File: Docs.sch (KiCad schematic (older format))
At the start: 0 parts

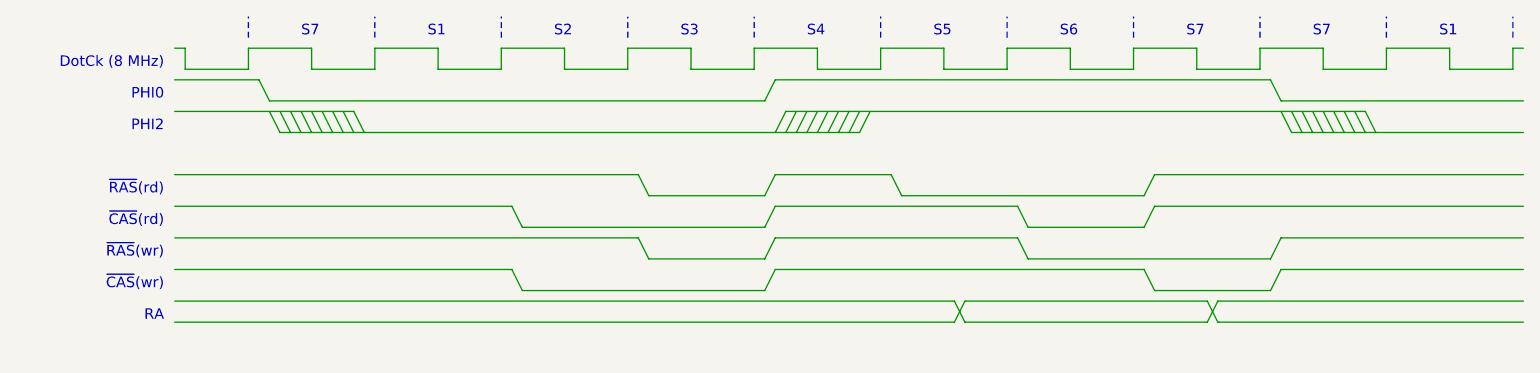
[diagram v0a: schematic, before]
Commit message: Updated timing diagram
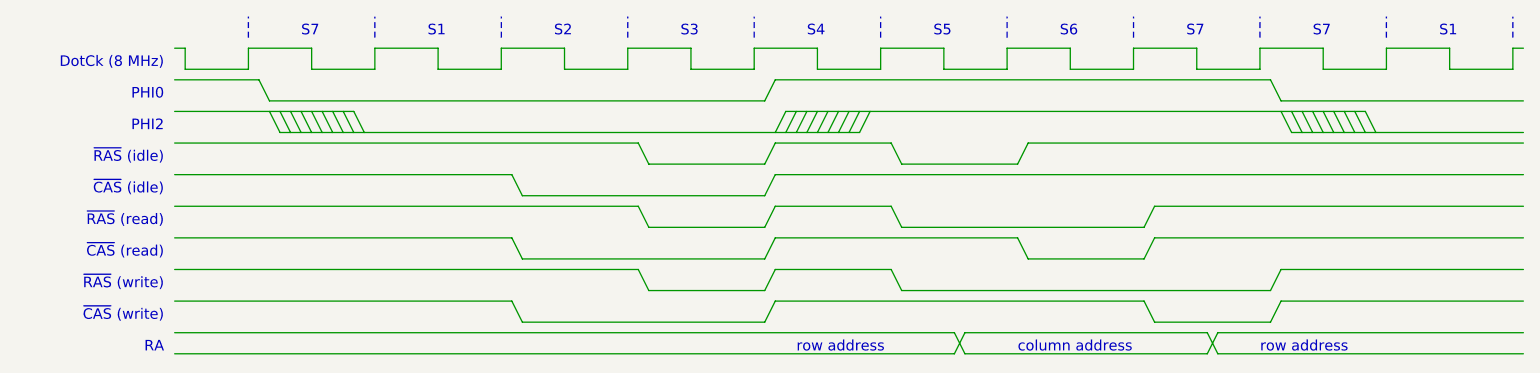
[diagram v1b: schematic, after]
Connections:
- wire segments 129 -> 143
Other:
- note added: "column address"
- note added: "row address"
- note added: "~CAS~ (idle)"
- note added: "~CAS~ (read)"
- note added: "~CAS~ (write)"
- note added: "~RAS~ (idle)"
- note added: "~RAS~ (read)"
- note added: "~RAS~ (write)"
- note removed: "~CAS~(rd)"
- note removed: "~CAS~(wr)"
- note removed: "~RAS~(rd)"
- note removed: "~RAS~(wr)"
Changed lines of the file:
@@
 Wire Wire Line
 	1100 1500 1950 1500
-Text Notes 1050 1900 2    50   ~ 0
-~RAS~(rd)
-Text Notes 1050 2050 2    50   ~ 0
-~CAS~(rd)
-Wire Wire Line
-	1100 1800 3300 1800
-Wire Wire Line
-	3300 1800 3350 1900
-Wire Wire Line
-	1100 1950 2700 1950
-Wire Wire Line
-	2700 1950 2750 2050
-Wire Wire Line
-	2750 2050 3900 2050
-Wire Wire Line
-	3900 2050 3950 1950
-Wire Wire Line
-	3350 1900 3900 1900
-Wire Wire Line
-	3900 1900 3950 1800
-Wire Wire Line
-	3950 1950 5100 1950
-Wire Wire Line
-	4500 1800 4550 1900
-Wire Wire Line
-	5100 1950 5150 2050
-Wire Wire Line
-	3950 1800 4500 1800
 Wire Notes Line
 	6850 1150 6850 1050
@@
 	6750 1500 6800 1600
 Wire Wire Line
-	5150 2050 5700 2050
-Wire Wire Line
-	5700 2050 5750 1950
-Wire Wire Line
-	4550 1900 5700 1900
-Wire Wire Line
-	5700 1900 5750 1800
-Text Notes 1050 2500 2    50   ~ 0
-RA
-Wire Wire Line
-	1100 2400 4800 2400
-Wire Wire Line
-	4800 2400 4850 2500
-Wire Wire Line
-	1100 2500 4800 2500
-Wire Wire Line
-	4800 2500 4850 2400
-Wire Wire Line
-	4850 2400 6000 2400
-Wire Wire Line
-	6000 2400 6050 2500
-Wire Wire Line
-	4850 2500 6000 2500
-Wire Wire Line
-	6050 2500 7500 2500
-Wire Wire Line
-	5750 1800 7500 1800
-Wire Wire Line
-	5750 1950 7500 1950
-Text Notes 1050 2200 2    50   ~ 0
-~RAS~(wr)
-Text Notes 1050 2350 2    50   ~ 0
-~CAS~(wr)
-Wire Wire Line
-	1100 2100 3300 2100
-Wire Wire Line
-	3300 2100 3350 2200
-Wire Wire Line
-	1100 2250 2700 2250
-Wire Wire Line
-	2700 2250 2750 2350
-Wire Wire Line
-	2750 2350 3900 2350
-Wire Wire Line
-	3900 2350 3950 2250
-Wire Wire Line
-	3350 2200 3900 2200
-Wire Wire Line
-	3900 2200 3950 2100
-Wire Wire Line
-	3950 2250 5700 2250
-Wire Wire Line
-	5700 2250 5750 2350
-Wire Wire Line
-	5750 2350 6300 2350
-Wire Wire Line
-	6300 2350 6350 2250
-Wire Wire Line
-	6300 2200 6350 2100
-Wire Wire Line
-	6350 2100 7500 2100
-Wire Wire Line
-	6350 2250 7500 2250
-Wire Wire Line
-	6050 2400 7500 2400
-Wire Wire Line
-	6000 2500 6050 2400
-Wire Wire Line
-	5150 2200 6300 2200
-Wire Wire Line
-	5100 2100 5150 2200
-Wire Wire Line
-	3950 2100 5100 2100
-Wire Wire Line
 	1700 1500 1750 1600
 Wire Wire Line
@@
 Wire Wire Line
 	6400 1600 7500 1600
+Wire Wire Line
+	3950 2250 4500 2250
+Wire Wire Line
+	4500 2250 4550 2350
+Wire Wire Line
+	4550 2350 6300 2350
+Wire Wire Line
+	6000 2650 6050 2550
+Wire Wire Line
+	6050 2550 7500 2550
+Wire Wire Line
+	6350 2400 7500 2400
+Wire Wire Line
+	6350 2250 7500 2250
+Wire Wire Line
+	6300 2350 6350 2250
+Wire Wire Line
+	6300 2500 6350 2400
+Wire Wire Line
+	5750 2500 6300 2500
+Wire Wire Line
+	5700 2400 5750 2500
+Wire Wire Line
+	3950 2400 5700 2400
+Wire Wire Line
+	3900 2350 3950 2250
+Wire Wire Line
+	3350 2350 3900 2350
+Wire Wire Line
+	3900 2500 3950 2400
+Wire Wire Line
+	2750 2500 3900 2500
+Wire Wire Line
+	2700 2400 2750 2500
+Wire Wire Line
+	1100 2400 2700 2400
+Wire Wire Line
+	3300 2250 3350 2350
+Wire Wire Line
+	1100 2250 3300 2250
+Text Notes 1050 2500 2    50   ~ 0
+~CAS~ (write)
+Text Notes 1050 2350 2    50   ~ 0
+~RAS~ (write)
+Wire Wire Line
+	5750 2100 7500 2100
+Wire Wire Line
+	5750 1950 7500 1950
+Wire Wire Line
+	6050 2650 7500 2650
+Wire Wire Line
+	4850 2650 6000 2650
+Wire Wire Line
+	6000 2550 6050 2650
+Wire Wire Line
+	4850 2550 6000 2550
+Wire Wire Line
+	4800 2650 4850 2550
+Wire Wire Line
+	1100 2650 4800 2650
+Wire Wire Line
+	4800 2550 4850 2650
+Wire Wire Line
+	1100 2550 4800 2550
+Text Notes 1050 2650 2    50   ~ 0
+RA
+Wire Wire Line
+	5700 2050 5750 1950
+Wire Wire Line
+	4550 2050 5700 2050
+Wire Wire Line
+	5700 2200 5750 2100
+Wire Wire Line
+	5150 2200 5700 2200
+Wire Wire Line
+	3950 1950 4500 1950
+Wire Wire Line
+	5100 2100 5150 2200
+Wire Wire Line
+	4500 1950 4550 2050
+Wire Wire Line
+	3950 2100 5100 2100
+Wire Wire Line
+	3900 2050 3950 1950
+Wire Wire Line
+	3350 2050 3900 2050
+Wire Wire Line
+	3900 2200 3950 2100
+Wire Wire Line
+	2750 2200 3900 2200
+Wire Wire Line
+	2700 2100 2750 2200
+Wire Wire Line
+	1100 2100 2700 2100
+Wire Wire Line
+	3300 1950 3350 2050
+Wire Wire Line
+	1100 1950 3300 1950
+Text Notes 1050 2200 2    50   ~ 0
+~CAS~ (read)
+Text Notes 1050 2050 2    50   ~ 0
+~RAS~ (read)
+Wire Wire Line
+	5150 1650 7500 1650
+Wire Wire Line
+	5100 1750 5150 1650
+Wire Wire Line
+	4550 1750 5100 1750
+Wire Wire Line
+	3950 1650 4500 1650
+Wire Wire Line
+	4500 1650 4550 1750
+Wire Wire Line
+	3900 1750 3950 1650
+Wire Wire Line
+	3350 1750 3900 1750
+Wire Wire Line
+	3900 1900 3950 1800
+Wire Wire Line
+	2750 1900 3900 1900
+Wire Wire Line
+	2700 1800 2750 1900
+Wire Wire Line
+	1100 1800 2700 1800
+Wire Wire Line
+	3300 1650 3350 1750
+Wire Wire Line
+	1100 1650 3300 1650
+Text Notes 1050 1750 2    50   ~ 0
+~RAS~ (idle)
+Text Notes 1050 1900 2    50   ~ 0
+~CAS~ (idle)
+Wire Wire Line
+	3950 1800 7500 1800
+Text Notes 4050 2650 0    50   ~ 0
+row address
+Text Notes 5100 2650 0    50   ~ 0
+column address
+Text Notes 6250 2650 0    50   ~ 0
+row address
 $EndSCHEMATC

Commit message: idk
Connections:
- wire segments 143 -> 247
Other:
- note added: "ACT"
- note added: "AREF"
- note added: "Command (read/idle)"
- note added: "Command (write)"
- note added: "NOP"
- note added: "PC all"
- note added: "PHI02r1"
- note added: "PHI02r2"
- note added: "PHI2e1"
- note added: "PHI2e2"
- note added: "PHI2e3"
- note added: "PHI2e4"
- note added: "PHI2e5"
- note added: "PHI2e6"
- note added: "PHI2e7"
- note added: "PHI2e8"
- note added: "RCS <= PHI2e7 || PHI2e8 || (Ref8 && (PHI2e3 || (PHI2e4 && IO1 && ~WE~) || (PHI2e5 && IO1 && WE)))\nRAS <= PHI2e7 || PHI2e8 || PHI2e3\nCAS <= PHI2e8 || (PHI2e4 && IO1 && ~WE~) || (PHI2e5 && IO1 && WE)\nWE <= PHI2e7 || (PHI2e8 && Ref0)\nDQM <= Ref8\nAmux <= PHI2e4 || PHI2e5\n\nAlwaysCS <= PHI2e7 || PHI2e8\nReadWriteCS <= (PHI2e4 && IO1 && ~WE~) || (PHI2e5 && IO1 && WE)\n\nRCS <= AlwaysCS || (Ref8 &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"
- note added: "RD"
- note added: "WR"
- note removed: "S1"
- note removed: "S2"
- note removed: "S3"
- note removed: "S4"
- note removed: "S5"
- note removed: "S6"
- note removed: "S7"
- note removed: "~CAS~ (idle)"
- note removed: "~CAS~ (read)"
- note removed: "~CAS~ (write)"
- note removed: "~RAS~ (idle)"
- note removed: "~RAS~ (read)"
- note removed: "~RAS~ (write)"
